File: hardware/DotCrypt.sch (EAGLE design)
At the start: 14 parts, among them CN1 1X4-BIG, U1 ATMEGA328P-MU-QFN32, U3 ATSHA204-TSU

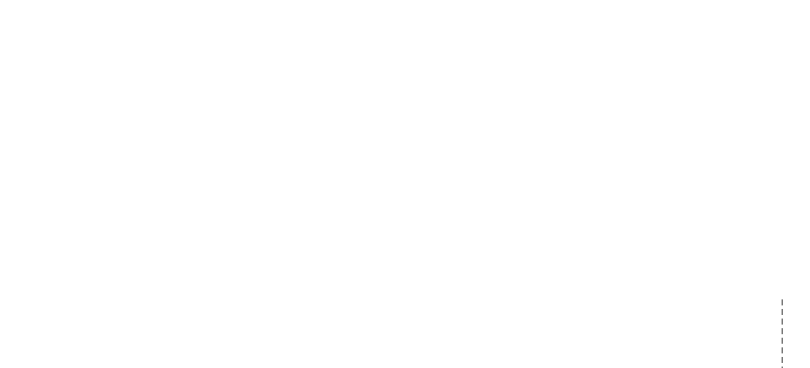
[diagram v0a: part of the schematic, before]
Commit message: Add OSHW logo, vTags, rearrange USB connections
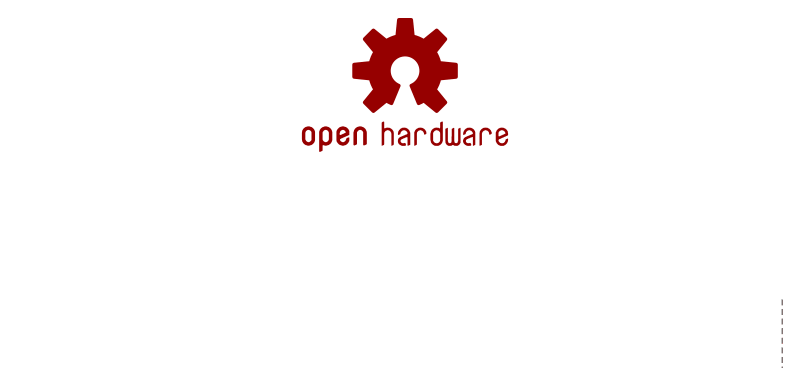
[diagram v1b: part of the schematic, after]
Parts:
- added LOGO1: OSHW-LOGOS, SparkFun-Aesthetics:OSHW-LOGOS
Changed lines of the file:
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@@
 <part name="JP3" library="Spark" deviceset="USB" device="PCB"/>
 <part name="+3V3" library="supply1" deviceset="+3V3" device=""/>
+<part name="LOGO1" library="SparkFun-Aesthetics" deviceset="OSHW-LOGO" device="S"/>
 </parts>
 <sheets>
@@
 <instance part="JP3" gate="G$1" x="210.82" y="73.66" rot="R180"/>
 <instance part="+3V3" gate="G$1" x="227.33" y="74.93"/>
+<instance part="LOGO1" gate="G$1" x="128.27" y="203.2"/>
 </instances>
 <busses>

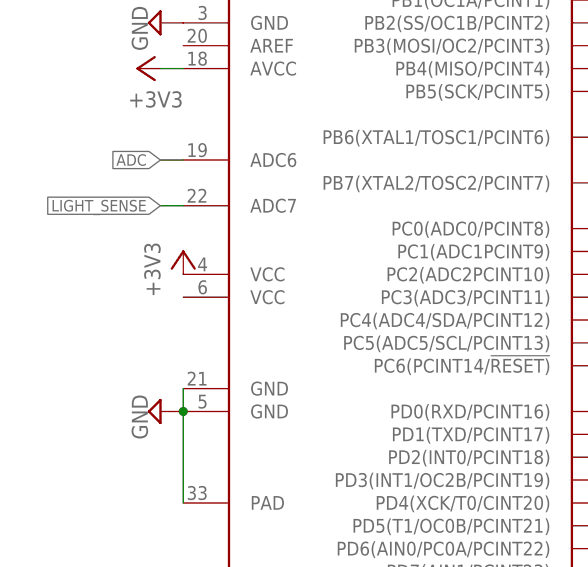
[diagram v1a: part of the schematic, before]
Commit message: Rearrange logos and pin connections
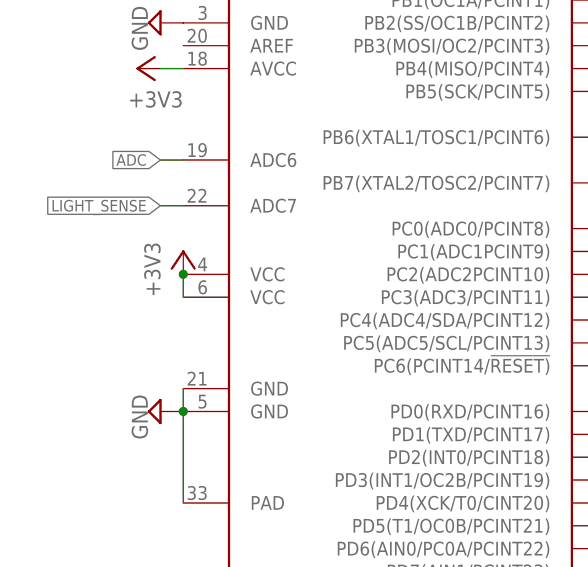
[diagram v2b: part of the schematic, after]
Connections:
- net +3V3: now also U1.VCC@2
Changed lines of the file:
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@@
 <setting verticaltext="up"/>
 </settings>
-<grid distance="0.05" unitdist="inch" unit="inch" style="lines" multiple="1" display="no" altdistance="0.01" altunitdist="inch" altunit="inch"/>
+<grid distance="0.1" unitdist="inch" unit="inch" style="lines" multiple="1" display="no" altdistance="0.01" altunitdist="inch" altunit="inch"/>
 <layers>
 <layer number="1" name="Top" color="4" fill="1" visible="no" active="no"/>
@@
 <pinref part="U1" gate="G$1" pin="VCC@1"/>
 <pinref part="+3V4" gate="G$1" pin="+3V3"/>
-</segment>
-<segment>
+<pinref part="U1" gate="G$1" pin="VCC@2"/>
+<wire x1="2.54" y1="134.62" x2="2.54" y2="137.16" width="0.1524" layer="91"/>
+<junction x="2.54" y="137.16"/>
+</segment>
+<segment>

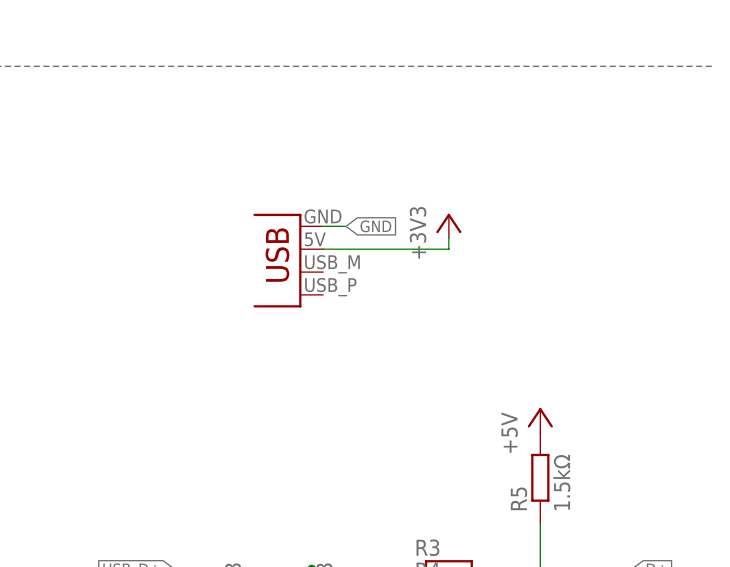
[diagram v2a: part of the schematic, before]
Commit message: Add USB D+ D- connections
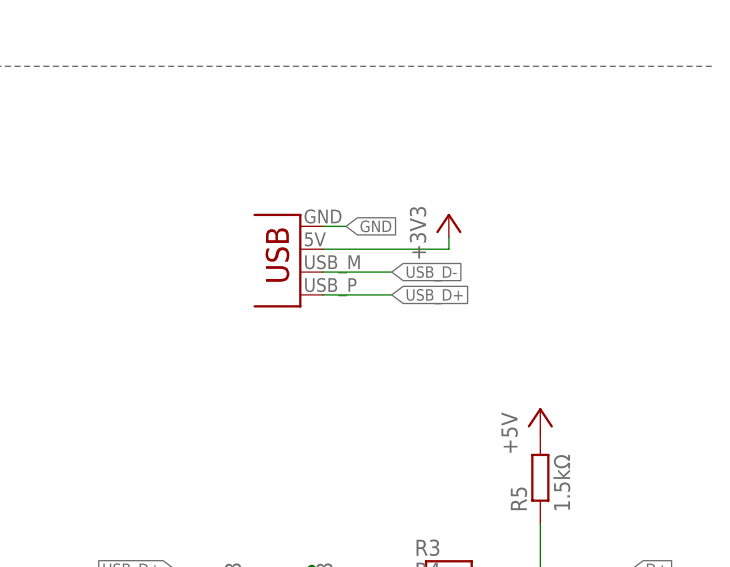
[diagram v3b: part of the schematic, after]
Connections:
- net USB_D+: now also JP3.D+
- net USB_D-: now also JP3.D-
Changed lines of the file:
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@@
 <pinref part="R4" gate="G$1" pin="1"/>
+</segment>
+<segment>
+<pinref part="JP3" gate="G$1" pin="D-"/>
+<wire x1="213.36" y1="68.58" x2="220.98" y2="68.58" width="0.1524" layer="91"/>
+<label x="220.98" y="68.58" size="1.27" layer="95" xref="yes"/>
 </segment>
 </net>
@@
 <pinref part="R3" gate="G$1" pin="1"/>
 </segment>
+<segment>
+<pinref part="JP3" gate="G$1" pin="D+"/>
+<wire x1="213.36" y1="66.04" x2="220.98" y2="66.04" width="0.1524" layer="91"/>
+<label x="220.98" y="66.04" size="1.27" layer="95" xref="yes"/>
+</segment>
 </net>

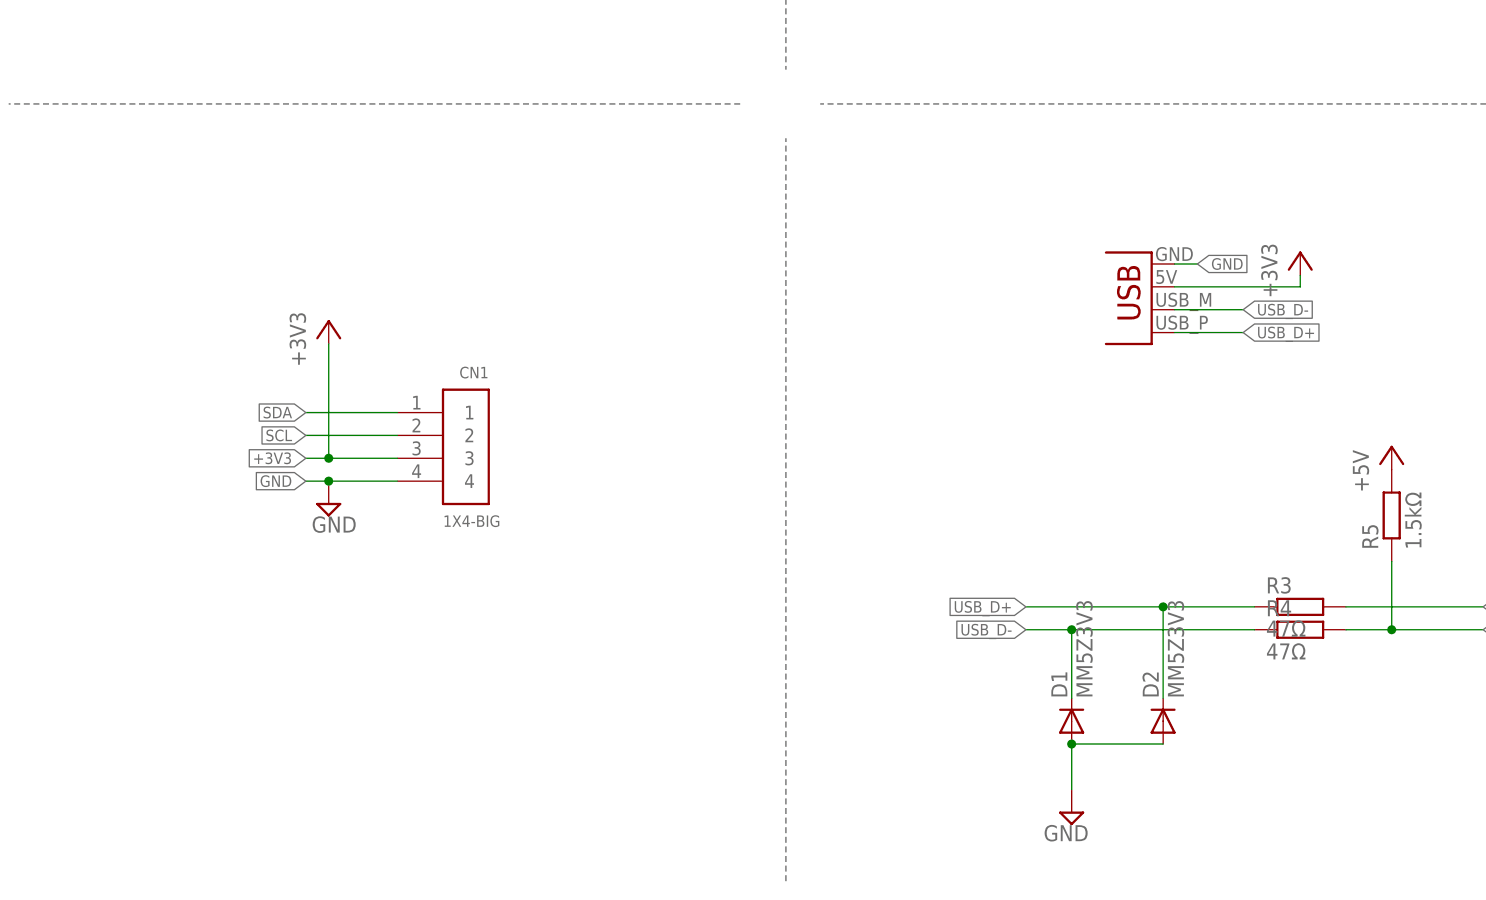
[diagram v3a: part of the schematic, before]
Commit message: Add 3V3 regulator
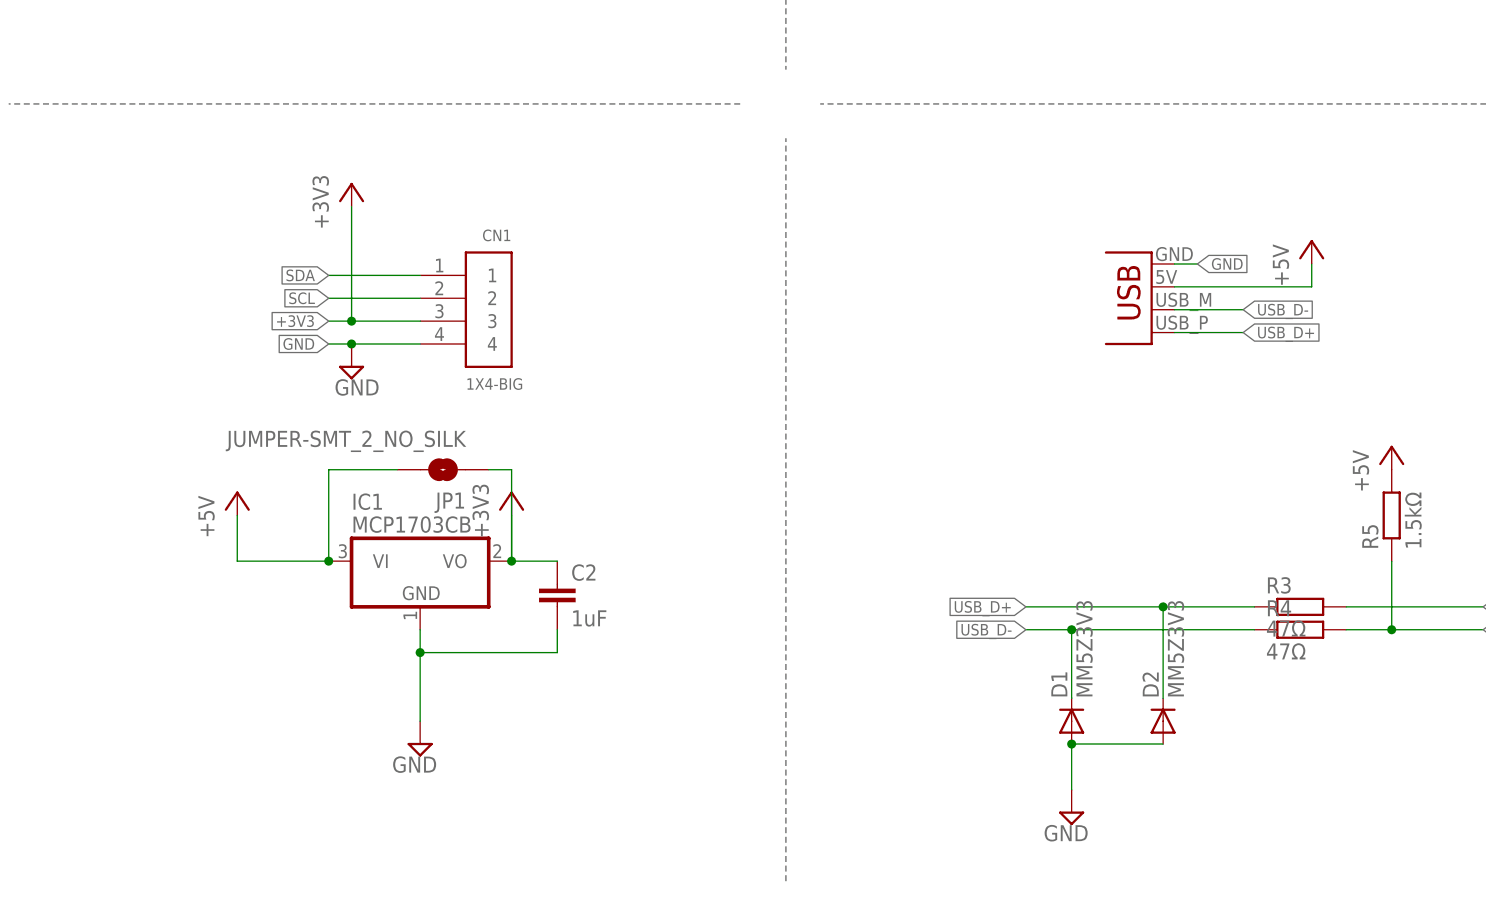
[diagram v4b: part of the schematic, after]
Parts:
- added C2: 1uF, rcl:C-EUC0603
- added IC1: MCP1703CB, linear:MCP1703CB
- added JP1: JUMPER-SMT_2_NO_SILK, SparkFun-Jumpers:JUMPER-SMT_2_NO_SILK
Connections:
- net +3V3: now also C2.1, IC1.VO, JP1.1; no longer JP3.VBUS
- net +5V: now also IC1.VI, JP1.2, JP3.VBUS
- net GND: now also C2.2, IC1.GND
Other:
- moved on the sheet: CN1
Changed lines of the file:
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@@
 <part name="P+1" library="supply1" deviceset="+5V" device=""/>
 <part name="JP3" library="Spark" deviceset="USB" device="PCB"/>
-<part name="+3V3" library="supply1" deviceset="+3V3" device=""/>
 <part name="LOGO1" library="SparkFun-Aesthetics" deviceset="OSHW-LOGO" device="S"/>
+<part name="SUPPLY1" library="supply2" deviceset="GND" device=""/>
+<part name="+3V5" library="supply1" deviceset="+3V3" device=""/>
+<part name="P+4" library="supply1" deviceset="+5V" device=""/>
+<part name="C2" library="rcl" deviceset="C-EU" device="C0603" value="1uF"/>
+<part name="IC1" library="linear" deviceset="MCP1703" device="CB"/>
+<part name="P+2" library="supply1" deviceset="+5V" device=""/>
+<part name="JP1" library="SparkFun-Jumpers" deviceset="JUMPER-SMT_2_NO" device="_SILK"/>
 </parts>
 <sheets>
@@
 <instance part="R2" gate="C" x="212.09" y="146.05" rot="R90"/>
 <instance part="R2" gate="D" x="232.41" y="146.05" rot="R90"/>
-<instance part="+3V1" gate="G$1" x="119.38" y="67.31"/>
-<instance part="SUPPLY18" gate="GND" x="119.38" y="46.99"/>
-<instance part="CN1" gate="G$1" x="132.08" y="54.61"/>
+<instance part="+3V1" gate="G$1" x="121.92" y="82.55"/>
+<instance part="SUPPLY18" gate="GND" x="121.92" y="62.23"/>
+<instance part="CN1" gate="G$1" x="134.62" y="69.85"/>
 <instance part="U3" gate="G$1" x="25.4" y="49.53"/>
 <instance part="+3V10" gate="G$1" x="38.1" y="54.61"/>
@@
 <instance part="P+1" gate="1" x="237.49" y="53.34"/>
 <instance part="JP3" gate="G$1" x="210.82" y="73.66" rot="R180"/>
-<instance part="+3V3" gate="G$1" x="227.33" y="74.93"/>
 <instance part="LOGO1" gate="G$1" x="128.27" y="203.2"/>
+<instance part="SUPPLY1" gate="GND" x="129.54" y="20.32" rot="MR0"/>
+<instance part="+3V5" gate="G$1" x="139.7" y="48.26"/>
+<instance part="P+4" gate="1" x="109.22" y="48.26"/>
+<instance part="C2" gate="G$1" x="144.78" y="38.1"/>
+<instance part="IC1" gate="G$1" x="129.54" y="40.64"/>
+<instance part="P+2" gate="1" x="228.6" y="76.2"/>
+<instance part="JP1" gate="G$1" x="132.08" y="50.8" rot="R180"/>
 </instances>
 <busses>
@@
 </segment>
 <segment>
-<wire x1="127" y1="49.53" x2="119.38" y2="49.53" width="0.1524" layer="91"/>
+<wire x1="129.54" y1="64.77" x2="121.92" y2="64.77" width="0.1524" layer="91"/>
 <pinref part="SUPPLY18" gate="GND" pin="GND"/>
-<wire x1="119.38" y1="49.53" x2="116.84" y2="49.53" width="0.1524" layer="91"/>
-<junction x="119.38" y="49.53"/>
-<label x="116.84" y="49.53" size="1.27" layer="95" rot="R180" xref="yes"/>
+<wire x1="121.92" y1="64.77" x2="119.38" y2="64.77" width="0.1524" layer="91"/>
+<junction x="121.92" y="64.77"/>
+<label x="119.38" y="64.77" size="1.27" layer="95" rot="R180" xref="yes"/>
 <pinref part="CN1" gate="G$1" pin="4"/>
 </segment>
@@
 <wire x1="213.36" y1="73.66" x2="215.9" y2="73.66" width="0.1524" layer="91"/>
 <label x="215.9" y="73.66" size="1.27" layer="95" xref="yes"/>
+</segment>
+<segment>
+<pinref part="SUPPLY1" gate="GND" pin="GND"/>
+<pinref part="C2" gate="G$1" pin="2"/>
+<wire x1="129.54" y1="22.86" x2="129.54" y2="30.48" width="0.1524" layer="91"/>
+<wire x1="129.54" y1="30.48" x2="144.78" y2="30.48" width="0.1524" layer="91"/>
+<wire x1="144.78" y1="30.48" x2="144.78" y2="33.02" width="0.1524" layer="91"/>
+<pinref part="IC1" gate="G$1" pin="GND"/>
+<wire x1="129.54" y1="33.02" x2="129.54" y2="30.48" width="0.1524" layer="91"/>
+<junction x="129.54" y="30.48"/>
 </segment>
 </net>
@@
 </segment>
 <segment>
-<wire x1="127" y1="57.15" x2="116.84" y2="57.15" width="0.1524" layer="91"/>
-<label x="116.84" y="57.15" size="1.27" layer="95" rot="R180" xref="yes"/>
+<wire x1="129.54" y1="72.39" x2="119.38" y2="72.39" width="0.1524" layer="91"/>
+<label x="119.38" y="72.39" size="1.27" layer="95" rot="R180" xref="yes"/>
 <pinref part="CN1" gate="G$1" pin="1"/>
 </segment>
@@
 </segment>
 <segment>
-<wire x1="127" y1="54.61" x2="116.84" y2="54.61" width="0.1524" layer="91"/>
-<label x="116.84" y="54.61" size="1.27" layer="95" rot="R180" xref="yes"/>
+<wire x1="129.54" y1="69.85" x2="119.38" y2="69.85" width="0.1524" layer="91"/>
+<label x="119.38" y="69.85" size="1.27" layer="95" rot="R180" xref="yes"/>
 <pinref part="CN1" gate="G$1" pin="2"/>
 </segment>
@@
 </segment>
 <segment>
-<wire x1="127" y1="52.07" x2="119.38" y2="52.07" width="0.1524" layer="91"/>
+<wire x1="129.54" y1="67.31" x2="121.92" y2="67.31" width="0.1524" layer="91"/>
 <pinref part="+3V1" gate="G$1" pin="+3V3"/>
-<wire x1="119.38" y1="52.07" x2="116.84" y2="52.07" width="0.1524" layer="91"/>
-<wire x1="119.38" y1="64.77" x2="119.38" y2="52.07" width="0.1524" layer="91"/>
-<junction x="119.38" y="52.07"/>
-<label x="116.84" y="52.07" size="1.27" layer="95" rot="R180" xref="yes"/>
+<wire x1="121.92" y1="67.31" x2="119.38" y2="67.31" width="0.1524" layer="91"/>
+<wire x1="121.92" y1="80.01" x2="121.92" y2="67.31" width="0.1524" layer="91"/>
+<junction x="121.92" y="67.31"/>
+<label x="119.38" y="67.31" size="1.27" layer="95" rot="R180" xref="yes"/>
 <pinref part="CN1" gate="G$1" pin="3"/>
 </segment>
@@
 </segment>
 <segment>
-<pinref part="JP3" gate="G$1" pin="VBUS"/>
-<pinref part="+3V3" gate="G$1" pin="+3V3"/>
-<wire x1="213.36" y1="71.12" x2="227.33" y2="71.12" width="0.1524" layer="91"/>
-<wire x1="227.33" y1="71.12" x2="227.33" y2="72.39" width="0.1524" layer="91"/>
+<pinref part="+3V5" gate="G$1" pin="+3V3"/>
+<wire x1="139.7" y1="45.72" x2="139.7" y2="40.64" width="0.1524" layer="91"/>
+<pinref part="C2" gate="G$1" pin="1"/>
+<wire x1="144.78" y1="40.64" x2="139.7" y2="40.64" width="0.1524" layer="91"/>
+<pinref part="IC1" gate="G$1" pin="VO"/>
+<junction x="139.7" y="40.64"/>
+<pinref part="JP1" gate="G$1" pin="1"/>
+<wire x1="137.16" y1="50.8" x2="139.7" y2="50.8" width="0.1524" layer="91"/>
+<wire x1="139.7" y1="50.8" x2="139.7" y2="40.64" width="0.1524" layer="91"/>
 </segment>
 </net>
@@
 <pinref part="P+1" gate="1" pin="+5V"/>
 </segment>
-</net>
+<segment>
+<pinref part="P+4" gate="1" pin="+5V"/>
+<wire x1="109.22" y1="45.72" x2="109.22" y2="40.64" width="0.1524" layer="91"/>
+<wire x1="109.22" y1="40.64" x2="119.38" y2="40.64" width="0.1524" layer="91"/>
+<pinref part="IC1" gate="G$1" pin="VI"/>
+<pinref part="JP1" gate="G$1" pin="2"/>
+<wire x1="127" y1="50.8" x2="119.38" y2="50.8" width="0.1524" layer="91"/>
+<wire x1="119.38" y1="50.8" x2="119.38" y2="40.64" width="0.1524" layer="91"/>
+<junction x="119.38" y="40.64"/>
+</segment>
+<segment>
+<pinref part="JP3" gate="G$1" pin="VBUS"/>
+<pinref part="P+2" gate="1" pin="+5V"/>
+<wire x1="213.36" y1="71.12" x2="228.6" y2="71.12" width="0.1524" layer="91"/>
+<wire x1="228.6" y1="71.12" x2="228.6" y2="73.66" width="0.1524" layer="91"/>
+</segment>
+</net>
